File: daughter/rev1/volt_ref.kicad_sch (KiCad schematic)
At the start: 26 parts, among them U12 ADR1001AEZ, U24 ADA4523-1BRMZ, U25 LT6202CS5

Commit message: Finish routing of daughterboard
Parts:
- added R76: 0, Resistor_SMD:R_0402_1005Metric, symbol Device:R_US
- U24: footprint RM-8_ADI -> myparts:RM-8_ADI
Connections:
- net adc_ref_out: now also R76.1; no longer C133.2, R49.1, R50.1, R74.1
- new net: C133.2, R49.1, R50.1, R74.1, R76.2
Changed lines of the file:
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@@
 	(wire
 		(pts
-			(xy 364.49 133.35) (xy 378.46 133.35)
+			(xy 364.49 133.35) (xy 374.65 133.35)
 		)
 		(stroke
@@
 	(wire
 		(pts
+			(xy 382.27 133.35) (xy 388.62 133.35)
+		)
+		(stroke
+			(width 0)
+			(type default)
+		)
+	)
+	(wire
+		(pts
 			(xy 158.75 118.11) (xy 158.75 125.73)
 		)
@@
 	(hierarchical_label "adc_ref_out"
 		(shape input)
-		(at 378.46 133.35 0)
+		(at 388.62 133.35 0)
 		(effects
 			(font
@@
 	)
 	(symbol
+		(lib_id "Device:R_US")
+		(at 378.46 133.35 270)
+		(unit 1)
+		(exclude_from_sim no)
+		(in_bom yes)
+		(on_board yes)
+		(dnp no)
+		(property "Reference" "R76"
+			(at 378.206 135.636 90)
+			(effects
+				(font
+					(size 1.27 1.27)
+				)
+			)
+		)
+		(property "Value" "0"
+			(at 378.206 137.414 90)
+			(effects
+				(font
+					(size 1.27 1.27)
+				)
+			)
+		)
+		(property "Footprint" "Resistor_SMD:R_0402_1005Metric"
+			(at 378.206 134.366 90)
+			(effects
+				(font
+					(size 1.27 1.27)
+				)
+				(hide yes)
+			)
+		)
+		(property "Datasheet" "~"
+			(at 378.46 133.35 0)
+			(effects
+				(font
+					(size 1.27 1.27)
+				)
+				(hide yes)
+			)
+		)
+		(property "Description" "RES 0805 2 OHM 0.1%"
+			(at 378.46 133.35 0)
+			(effects
+				(font
+					(size 1.27 1.27)
+				)
+				(hide yes)
+			)
+		)
+		(property "Tolerance" "0.1%"
+			(at 378.46 130.302 0)
+			(effects
+				(font
+					(size 1.27 1.27)
+				)
+				(hide yes)
+			)
+		)
+		(property "MFG" "Stackpole"
+			(at 378.46 133.35 90)
+			(effects
+				(font
+					(size 1.27 1.27)
+				)
+				(hide yes)
+			)
+		)
+		(property "MFG_PN" "RNCA0805BTS2K00"
+			(at 378.46 133.35 90)
+			(effects
+				(font
+					(size 1.27 1.27)
+				)
+				(hide yes)
+			)
+		)
+		(pin "2"
+		)
+		(pin "1"
+		)
+		(instances
+			(project "psc_daughter_brd"
+				(path "/40891cc8-bf64-41f4-8f69-a607d7b280eb/dea95122-986e-41c8-b99e-e429cc6f4cd5/4999e499-3966-4a05-8928-c40234f9b048"
+					(reference "R76")
+					(unit 1)
+				)
+			)
+		)
+	)
+	(symbol
 		(lib_id "power:GND")
 		(at 238.76 128.27 0)
@@
 			)
 		)
-		(property "Footprint" "RM-8_ADI"
+		(property "Footprint" "myparts:RM-8_ADI"
 			(at 284.48 133.35 0)
 			(effects
@@
 		)
 		(instances
-			(project ""
+			(project "psc_daughter_brd"
 				(path "/40891cc8-bf64-41f4-8f69-a607d7b280eb/dea95122-986e-41c8-b99e-e429cc6f4cd5/4999e499-3966-4a05-8928-c40234f9b048"
 					(reference "U24")

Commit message: Rename versions
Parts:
- removed C124, C131, C135: 0.1uF, Capacitor_SMD:C_0402_1005Metric, symbol Device:C_Small
- removed C125: 4.7uF, Capacitor_SMD:C_0402_1005Metric, symbol Device:C_Small
- removed C126, C134: 10uF, Capacitor_SMD:C_0603_1608Metric, symbol Device:C_Small
- removed C132: 47nF, Capacitor_SMD:C_0402_1005Metric, symbol Device:C_Small
- removed C133: 47uF, Capacitor_SMD:C_1210_3225Metric, symbol Device:C_Small
- removed R49: 1K, Resistor_SMD:R_0402_1005Metric, symbol Device:R_US
- removed R50: 2, Resistor_SMD:R_0402_1005Metric, symbol Device:R_US
- removed R74: 750, Resistor_SMD:R_0402_1005Metric, symbol Device:R_US
- removed R75: 5.62k, Resistor_SMD:R_0402_1005Metric, symbol Device:R_US
- removed R76: 0, Resistor_SMD:R_0402_1005Metric, symbol Device:R_US
- removed U24: ADA4523-1BRMZ, myparts:RM-8_ADI, symbol ADA4523:ADA4523-1BRMZ
- removed U25: LT6202CS5, myparts:LT6202CS5, symbol PSC:LT6202CS5
- U12: footprint myparts:E-20-1_ADI -> E-20-1_ADI
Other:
- note removed: "DNP use cap if needed"
- moved on the sheet: C32, C50, C51, C52

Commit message: Change adc driver to ADA4945
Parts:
- U12: footprint E-20-1_ADI -> myparts:E-20-1_ADI
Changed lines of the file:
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@@
 		)
 		(instances
-			(project ""
+			(project "psc_daughter_brd"
 				(path "/40891cc8-bf64-41f4-8f69-a607d7b280eb/dea95122-986e-41c8-b99e-e429cc6f4cd5/4999e499-3966-4a05-8928-c40234f9b048"
 					(reference "#PWR077")
@@
 			)
 		)
-		(property "Footprint" "E-20-1_ADI"
+		(property "Footprint" "myparts:E-20-1_ADI"
 			(at 180.34 97.79 0)
 			(effects
@@
 		)
 		(instances
-			(project ""
+			(project "psc_daughter_brd"
 				(path "/40891cc8-bf64-41f4-8f69-a607d7b280eb/dea95122-986e-41c8-b99e-e429cc6f4cd5/4999e499-3966-4a05-8928-c40234f9b048"
 					(reference "U12")

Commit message: linked ADR1001 to DCCT ADC reference for 5V and 2.5V
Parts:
- added C124, C131, C135: 0.1uF, Capacitor_SMD:C_0402_1005Metric, symbol Device:C_Small
- added C125: 4.7uF, Capacitor_SMD:C_0402_1005Metric, symbol Device:C_Small
- added C126, C134: 10uF, Capacitor_SMD:C_0603_1608Metric, symbol Device:C_Small
- added C132: 47nF, Capacitor_SMD:C_0402_1005Metric, symbol Device:C_Small
- added C133: 47uF, Capacitor_SMD:C_1210_3225Metric, symbol Device:C_Small
- added R49: 1K, Resistor_SMD:R_0402_1005Metric, symbol Device:R_US
- added R50: 2, Resistor_SMD:R_0402_1005Metric, symbol Device:R_US
- added R74: 750, Resistor_SMD:R_0402_1005Metric, symbol Device:R_US
- added R75: 5.62k, Resistor_SMD:R_0402_1005Metric, symbol Device:R_US
- added U24: ADA4523-1BRMZ, RM-8_ADI, symbol ADA4523:ADA4523-1BRMZ
- added U25: LT6202CS5, myparts:LT6202CS5, symbol PSC:LT6202CS5
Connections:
- net +15V: now also C126.1, C131.1, C134.1, C135.1, U24.7 (V+), U25.5 (V+)
- net GND: now also C126.2, C131.2, C133.1, C134.2, C135.2, U24.4 (V-), U25.2 (V-)
- net at C32.1, U12.10 (VDOUT), U12.11 (BUF_INP): now also U24.3 (+)
- new net: C125.1, R49.2, U24.2 (-)
- new net: C125.2, U24.6, U25.3 (+)
- new net: C132.1, R75.1
- new net: C132.2, R50.2, U25.1
- new net: R49.1, R74.1
- new net: R74.2, R75.2, U25.4 (-)
- new net: C124.1, U24.1 (*SD)
- new net: C124.2, U24.8 (SDC)
- new net adc_ref_out: C133.2, R50.1
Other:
- moved on the sheet: C32, C50, C51, C52

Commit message: was missing feedback on adc_ref_out page 4
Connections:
- net adc_ref_out: now also R49.1, R74.1
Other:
- moved on the sheet: C133
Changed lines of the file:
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@@
 	)
 	(junction
-		(at 358.14 133.35)
+		(at 364.49 133.35)
 		(diameter 0)
 		(color 0 0 0 0)
@@
 	)
 	(junction
+		(at 320.04 154.94)
+		(diameter 0)
+		(color 0 0 0 0)
+	)
+	(junction
 		(at 320.04 144.78)
 		(diameter 0)
@@
 	)
 	(junction
+		(at 356.87 133.35)
+		(diameter 0)
+		(color 0 0 0 0)
+	)
+	(junction
 		(at 157.48 85.09)
 		(diameter 0)
@@
 	(wire
 		(pts
+			(xy 320.04 154.94) (xy 356.87 154.94)
+		)
+		(stroke
+			(width 0)
+			(type default)
+		)
+	)
+	(wire
+		(pts
 			(xy 297.18 120.65) (xy 297.18 118.11)
 		)
@@
 	(wire
 		(pts
-			(xy 358.14 133.35) (xy 372.11 133.35)
+			(xy 364.49 133.35) (xy 378.46 133.35)
 		)
 		(stroke
@@
 	(wire
 		(pts
+			(xy 356.87 154.94) (xy 356.87 133.35)
+		)
+		(stroke
+			(width 0)
+			(type default)
+		)
+	)
+	(wire
+		(pts
 			(xy 149.86 113.03) (xy 149.86 127)
 		)
@@
 	(wire
 		(pts
-			(xy 358.14 140.97) (xy 358.14 139.7)
+			(xy 364.49 140.97) (xy 364.49 139.7)
 		)
 		(stroke
@@
 	(wire
 		(pts
+			(xy 356.87 133.35) (xy 364.49 133.35)
+		)
+		(stroke
+			(width 0)
+			(type default)
+		)
+	)
+	(wire
+		(pts
 			(xy 251.46 129.54) (xy 251.46 107.95)
 		)
@@
 	(wire
 		(pts
-			(xy 354.33 133.35) (xy 358.14 133.35)
+			(xy 354.33 133.35) (xy 356.87 133.35)
 		)
 		(stroke
@@
 	(wire
 		(pts
-			(xy 358.14 133.35) (xy 358.14 134.62)
+			(xy 364.49 133.35) (xy 364.49 134.62)
 		)
 		(stroke
@@
 	(hierarchical_label "adc_ref_out"
 		(shape input)
-		(at 372.11 133.35 0)
+		(at 378.46 133.35 0)
 		(effects
 			(font
@@
 	(symbol
 		(lib_id "Device:C_Small")
-		(at 358.14 137.16 180)
+		(at 364.49 137.16 180)
 		(unit 1)
 		(exclude_from_sim no)
@@
 		(dnp no)
 		(property "Reference" "C133"
-			(at 360.68 135.636 0)
+			(at 367.03 135.636 0)
 			(effects
 				(font
@@
 		)
 		(property "Value" "47uF"
-			(at 360.68 137.922 0)
+			(at 367.03 137.922 0)
 			(effects
 				(font
@@
 		)
 		(property "Footprint" "Capacitor_SMD:C_1210_3225Metric"
-			(at 358.14 137.16 0)
+			(at 364.49 137.16 0)
 			(effects
 				(font
@@
 		)
 		(property "Datasheet" "~"
-			(at 358.14 137.16 0)
+			(at 364.49 137.16 0)
 			(effects
 				(font
@@
 		)
 		(property "Description" "CAP CER 047UF 25V X5R 1210"
-			(at 358.14 137.16 0)
+			(at 364.49 137.16 0)
 			(effects
 				(font
@@
 		)
 		(property "Type" ""
-			(at 362.458 136.906 0)
+			(at 368.808 136.906 0)
 			(effects
 				(font
@@
 		)
 		(property "MFG" "Taiyo Yuden"
-			(at 358.14 137.16 0)
+			(at 364.49 137.16 0)
 			(effects
 				(font
@@
 		)
 		(property "MFG_PN" "MLAST32MAB5476MPNDT1"
-			(at 358.14 137.16 0)
+			(at 364.49 137.16 0)
 			(effects
 				(font
@@
 	(symbol
 		(lib_id "power:GND")
-		(at 358.14 140.97 0)
+		(at 364.49 140.97 0)
 		(unit 1)
 		(exclude_from_sim no)
@@
 		(fields_autoplaced yes)
 		(property "Reference" "#PWR0243"
-			(at 358.14 147.32 0)
+			(at 364.49 147.32 0)
 			(effects
 				(font
@@
 		)
 		(property "Value" "GND"
-			(at 358.14 146.05 0)
+			(at 364.49 146.05 0)
 			(effects
 				(font
@@
 		)
 		(property "Footprint" ""
-			(at 358.14 140.97 0)
+			(at 364.49 140.97 0)
 			(effects
 				(font
@@
 		)
 		(property "Datasheet" ""
-			(at 358.14 140.97 0)
+			(at 364.49 140.97 0)
 			(effects
 				(font
@@
 		)
 		(property "Description" "Power symbol creates a global label with name \"GND\" , ground"
-			(at 358.14 140.97 0)
+			(at 364.49 140.97 0)
 			(effects
 				(font

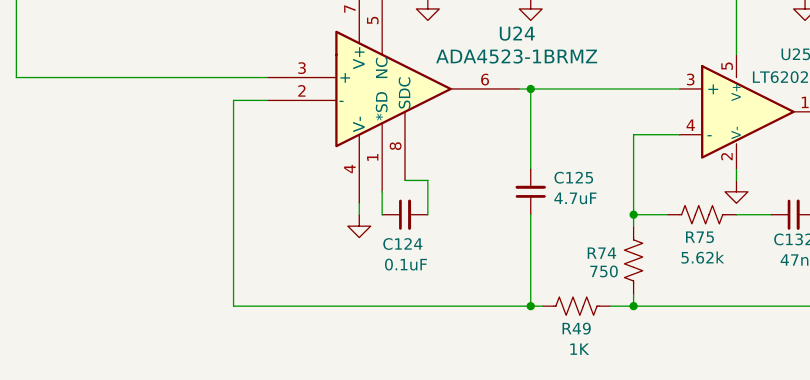
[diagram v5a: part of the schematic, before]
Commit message: added DNP note for cap on ADA4523-1
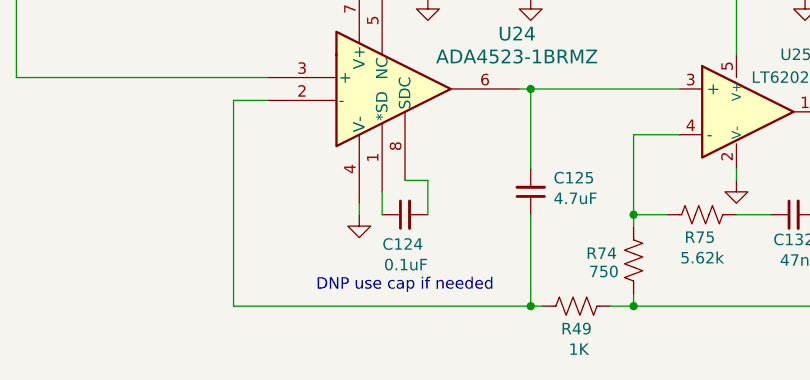
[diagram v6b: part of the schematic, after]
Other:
- note added: "DNP use cap if needed"
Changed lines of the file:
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@@
+		)
+	)
+	(text "DNP use cap if needed\n"
+		(exclude_from_sim no)
+		(at 294.64 152.654 0)
+		(effects
+			(font
+				(size 1.27 1.27)
+			)
 		)
 	)
